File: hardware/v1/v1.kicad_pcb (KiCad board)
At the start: 2 copper layers, 120 x 100 mm, 69 parts, among them J1 AUDIO IN, J2 MIDI OUT, J3 MIDI IN, J4 MIDI THRU, J5 OUTPUT R, J6 OUTPUT L - MONO, J7 EXP 2, J8 EXP 1, J9 Conn_01x02_Female, SW1 RotaryEncoder_Switch, U1 PT8211-pt8211, U2 Pico, U3 2.4inches, U4 TL074, U5 TL074, U6 TL072, U7 6N138

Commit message: started PCB
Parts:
- C1, C10, C11, C12, C13, C14, C15, C16, C17, C18, C19, C2, C20, C21, C22, C23, C24, C4, C5, C6, C7, C8, C9, D1, J7, J8, R1, R10, R11, R12, R13, R14, R15, R16, R17, R18, R19, R2, R20, R3, R4, R5, R6, R7, R8, R9, U4, U5, U6, U7: moved to B.Cu
- J9: footprint Connector_JST:JST_XH_B2B-XH-AM_1x02_P2.50mm_Vertical -> Connector_JST:JST_XH_B2B-XH-A_1x02_P2.50mm_Vertical
- moved U7 351.4 mm to (125.1, 72.7), turned to 180 degrees
- moved AudioIn_gain_trim_R_1 317.8 mm to (118.5, 118.8)
- moved D1 317.1 mm to (127.8, 72.7), turned to -90 degrees
- moved C24 308.9 mm to (114.6, 80.5), turned to 90 degrees
- moved RV_gain_trim_L_1 296.7 mm to (159.0, 67.8)
- moved R10 261.9 mm to (185.3, 92.0), turned to 180 degrees
- moved C12 249.3 mm to (185.6, 88.1), turned to 180 degrees
- moved R12 248.7 mm to (196.3, 66.5), turned to 180 degrees
- moved U4 248.5 mm to (185.5, 69.5), turned to 180 degrees
- moved C1 247.0 mm to (148.2, 108.0), turned to 180 degrees
- moved U6 244.4 mm to (140.7, 104.8)
- moved C11 238.5 mm to (196.3, 88.1), turned to 180 degrees
- moved RV_gain_trim_R_1 221.0 mm to (205.5, 62.8)
- moved U5 192.5 mm to (196.3, 69.5), turned to 180 degrees
- moved R2 183.5 mm to (496.4, 141.9), turned to 180 degrees
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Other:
- board size 120 x 100 mm -> 140 x 100 mm
- board text added: "Batteries (4xAA)"

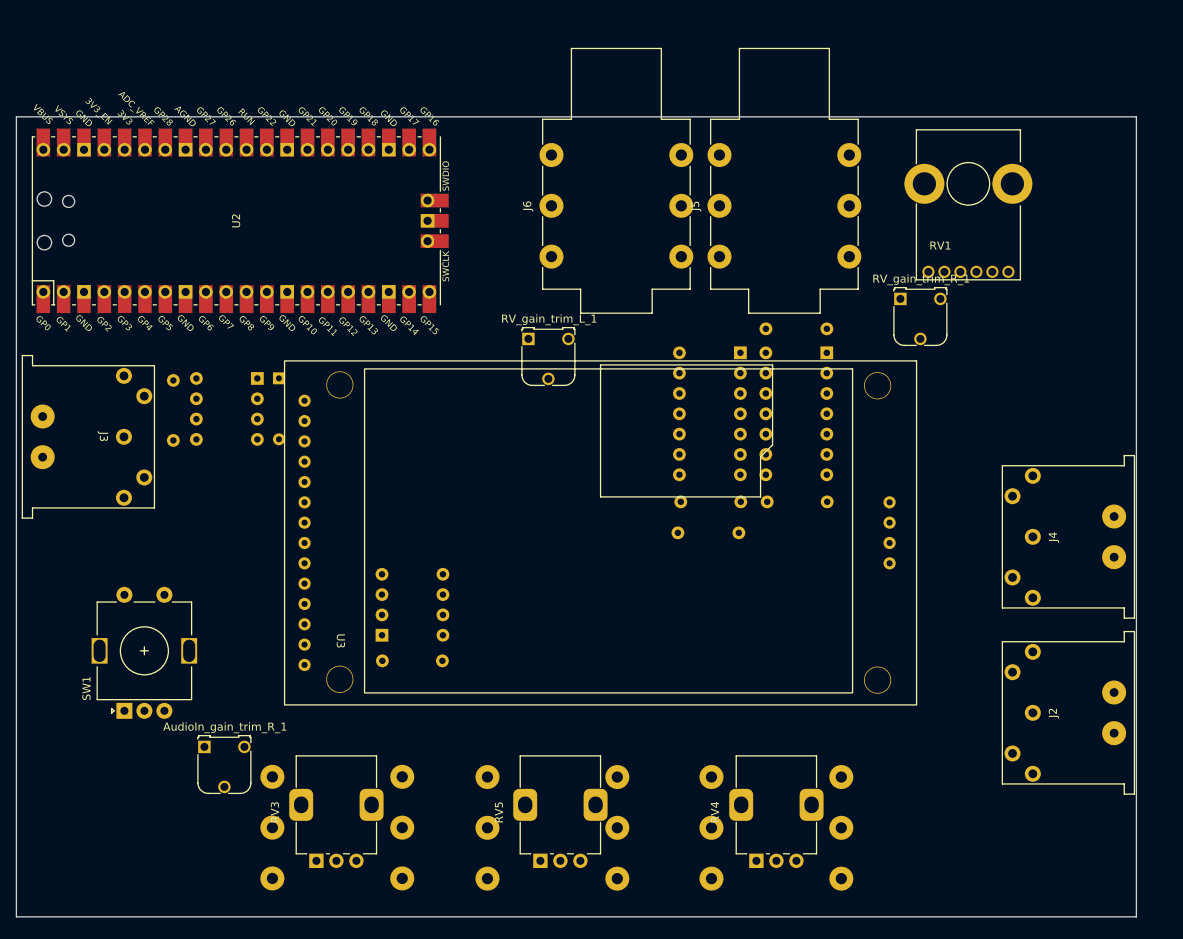
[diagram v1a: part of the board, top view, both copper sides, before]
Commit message: Shifted all connectors to B-side
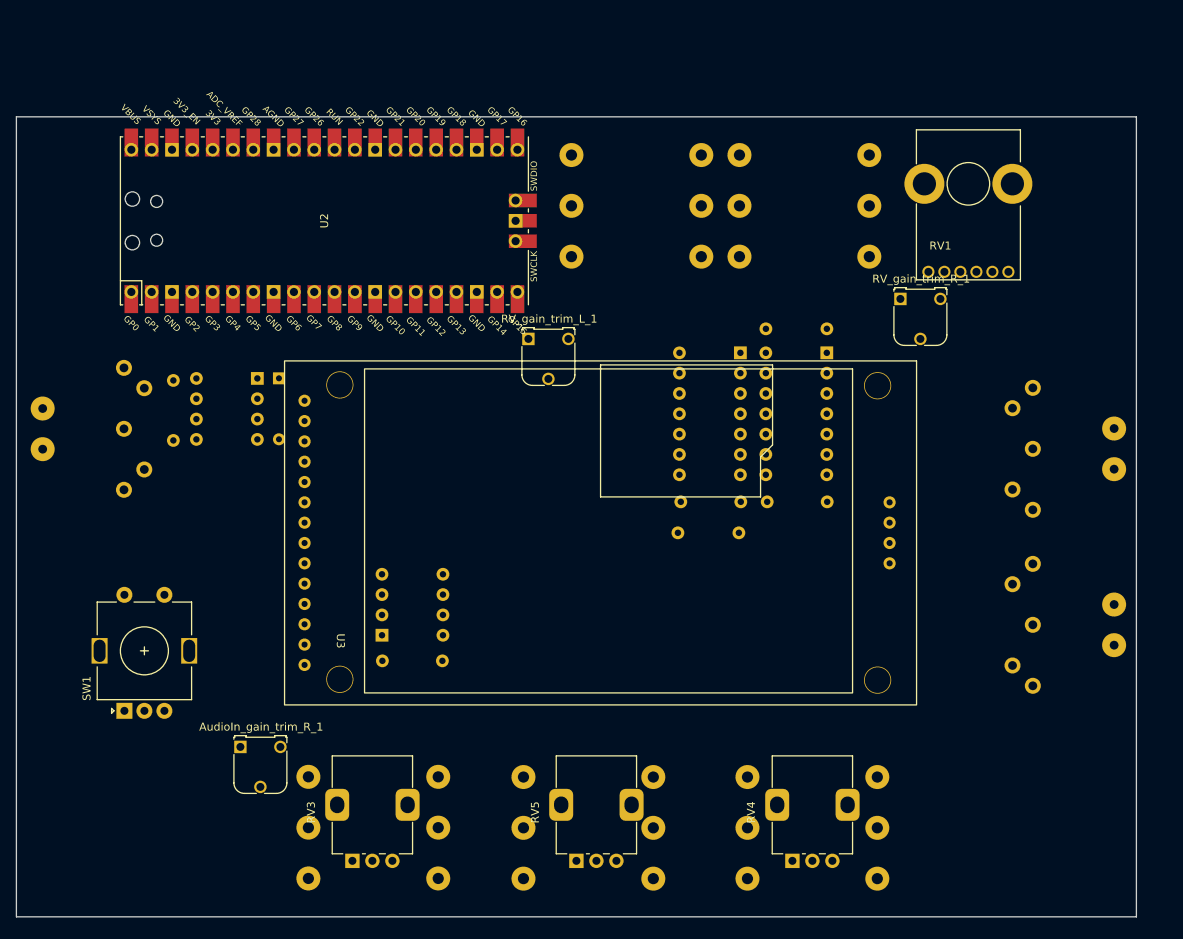
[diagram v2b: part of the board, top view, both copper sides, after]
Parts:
- J2, J3, J4, J5, J6: moved to B.Cu
- moved J5 18.7 mm to (201.6, 57.5)
- moved J6 18.7 mm to (180.6, 57.5)
- moved J2 11.0 mm to (222.1, 103.5), turned to -90 degrees
- moved J4 11.0 mm to (222.1, 81.5), turned to -90 degrees
- moved U2 11.0 mm to (133.5, 53.0)
- moved AudioIn_gain_trim_R_1 4.50 mm to (123.0, 118.8)
- moved J1 4.50 mm to (131.5, 122.5)
- moved J7 4.50 mm to (186.4, 122.5)
- moved J8 4.50 mm to (158.4, 122.5)
- moved RV3 4.50 mm to (137.0, 133.0)
- moved RV4 4.50 mm to (192.0, 133.0)
- moved RV5 4.50 mm to (165.0, 133.0)
- moved J3 1.00 mm to (108.4, 79.0), turned to 90 degrees

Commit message: Continued PCB placing
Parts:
- J9: value Conn_01x02_Female -> Batt In
- moved R13 297.9 mm to (175.8, 67.0)
- moved C23 294.7 mm to (122.2, 86.5)
- moved R18 294.6 mm to (125.3, 69.0)
- moved R7 264.7 mm to (163.5, 74.0), turned to -90 degrees
- moved C14 255.9 mm to (164.0, 88.0), turned to 0 degrees
- moved R9 252.4 mm to (166.5, 74.0), turned to -90 degrees
- moved C16 244.0 mm to (166.2, 84.5)
- moved R15 240.3 mm to (215.5, 107.7), turned to -90 degrees
- moved R20 239.0 mm to (216.0, 66.0), turned to -90 degrees
- moved R16 226.1 mm to (215.5, 105.3), turned to 90 degrees
- moved R6 223.9 mm to (184.0, 74.0), turned to -90 degrees
- moved C10 220.2 mm to (166.5, 91.5)
- moved C15 213.3 mm to (187.7, 84.5)
- moved C21 201.0 mm to (154.3, 105.5), turned to 0 degrees
- moved C13 190.6 mm to (184.9, 87.9), turned to 0 degrees
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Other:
- board text added: "1 - A"
- board text added: "1 - B"
- board text added: "2 - A"
- board text added: "2 - B"
- board text added: "3 - A"
- board text added: "3 - B"

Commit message: First draft on PCB placing
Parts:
- added G***: LOGO, PCB_symbols:owl_F_50x70, F.Cu at (60.5, 175.5)
- C3, U1: moved to B.Cu
- moved R14 330.1 mm to (148.3, 94.0)
- moved R2 322.7 mm to (181.0, 74.0), turned to -90 degrees
- moved R17 313.6 mm to (114.5, 83.3), turned to -90 degrees
- moved R3 297.7 mm to (190.2, 105.5), turned to 0 degrees
- moved C3 290.7 mm to (166.6, 107.5), turned to 0 degrees
- moved U1 283.2 mm to (170.5, 103.0), turned to 180 degrees
- moved R11 233.3 mm to (223.3, 69.8), turned to 90 degrees
- moved C8 217.5 mm to (188.0, 95.0)
- moved R5 217.2 mm to (197.8, 108.9)
- moved R1 205.8 mm to (190.2, 102.0), turned to 0 degrees
- moved C5 192.5 mm to (171.0, 92.8), turned to -90 degrees
- moved C2 191.8 mm to (184.9, 106.5)
- moved C7 186.4 mm to (177.0, 92.8), turned to -90 degrees
- moved C6 149.1 mm to (193.5, 93.0), turned to -90 degrees
- moved C4 147.7 mm to (199.4, 92.9), turned to -90 degrees
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
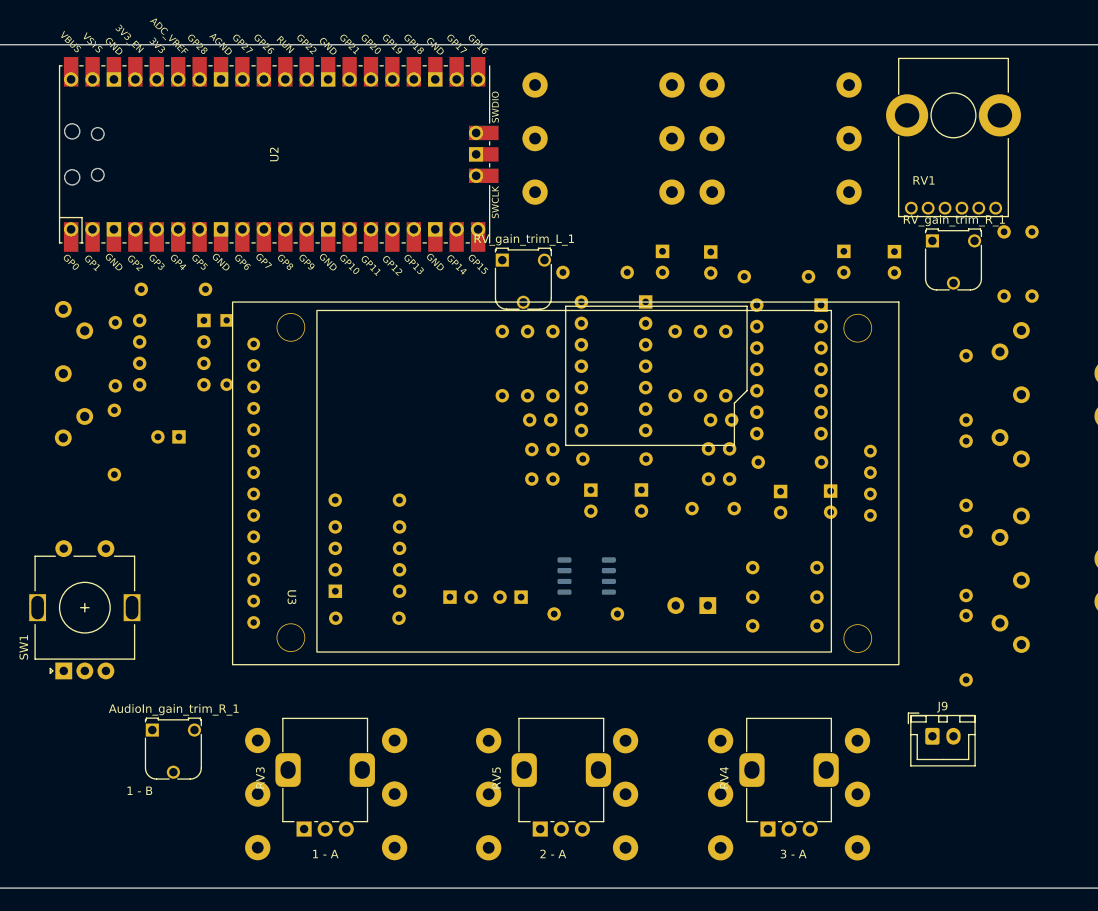
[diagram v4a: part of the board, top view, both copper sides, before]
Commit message: Added mounting holes - Cleaned PCB placement
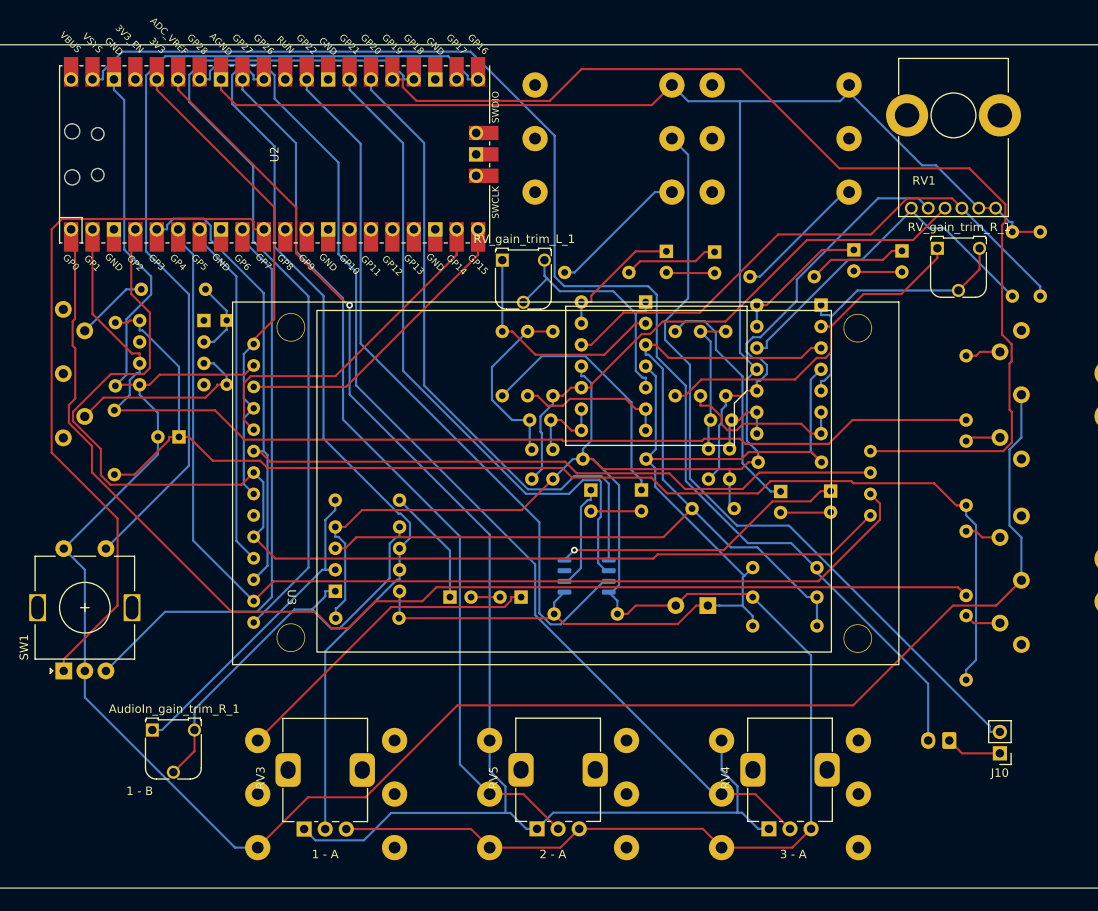
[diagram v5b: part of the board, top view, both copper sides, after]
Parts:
- added J10: Close for battery power, Connector_PinHeader_2.54mm:PinHeader_1x02_P2.54mm_Vertical, F.Cu at (219.5, 124.0)
- J9: moved to B.Cu
- moved J9 2.06 mm to (213.5, 122.5), turned to 180 degrees
- moved C17 1.20 mm to (202.2, 64.3)
- moved RV_gain_trim_R_1 1.06 mm to (212.1, 64.1)
- moved R10 0.98 mm to (221.0, 69.8)
- moved R11 0.98 mm to (224.3, 69.8)
- moved C18 0.89 mm to (207.9, 64.4)
- moved R12 0.68 mm to (197.5, 67.5)
- moved C22 0.45 mm to (185.7, 64.6)
- moved C19 0.45 mm to (180.0, 64.5)
- moved RV5 0.38 mm to (164.6, 133.0)
- moved R13 0.20 mm to (175.5, 67.0)
- moved J7 0.12 mm to (186.5, 122.5)
- moved J8 0.12 mm to (159.0, 122.5)
- moved RV4 0.12 mm to (192.1, 133.0)
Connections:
- J6 pad R: batt- -> Net-(J6-PadR)
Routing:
- net GNDA: track 0.00 -> 366.0 mm
- net GND: track 0.00 -> 255.7 mm
- net ADC_VREF: track 0.00 -> 171.9 mm, vias 0 -> 1
- net batt+: track 0.00 -> 159.9 mm
- net +3.3V: track 0.00 -> 148.2 mm
- net Net-(R16-Pad1): track 0.00 -> 144.4 mm
- net Net-(U2-Pad4): track 0.00 -> 141.8 mm
- net Net-(U2-Pad5): track 0.00 -> 130.0 mm
- net Net-(R17-Pad1): track 0.00 -> 129.8 mm
- net Net-(U2-Pad6): track 0.00 -> 129.6 mm
- net Net-(U2-Pad25): track 0.00 -> 128.8 mm
- net Net-(J7-PadR): track 0.00 -> 128.2 mm
- net filtered_vcc: track 0.00 -> 120.9 mm
- net virtual_mass: track 0.00 -> 110.7 mm
- net Net-(RV3-Pad2): track 0.00 -> 107.5 mm
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
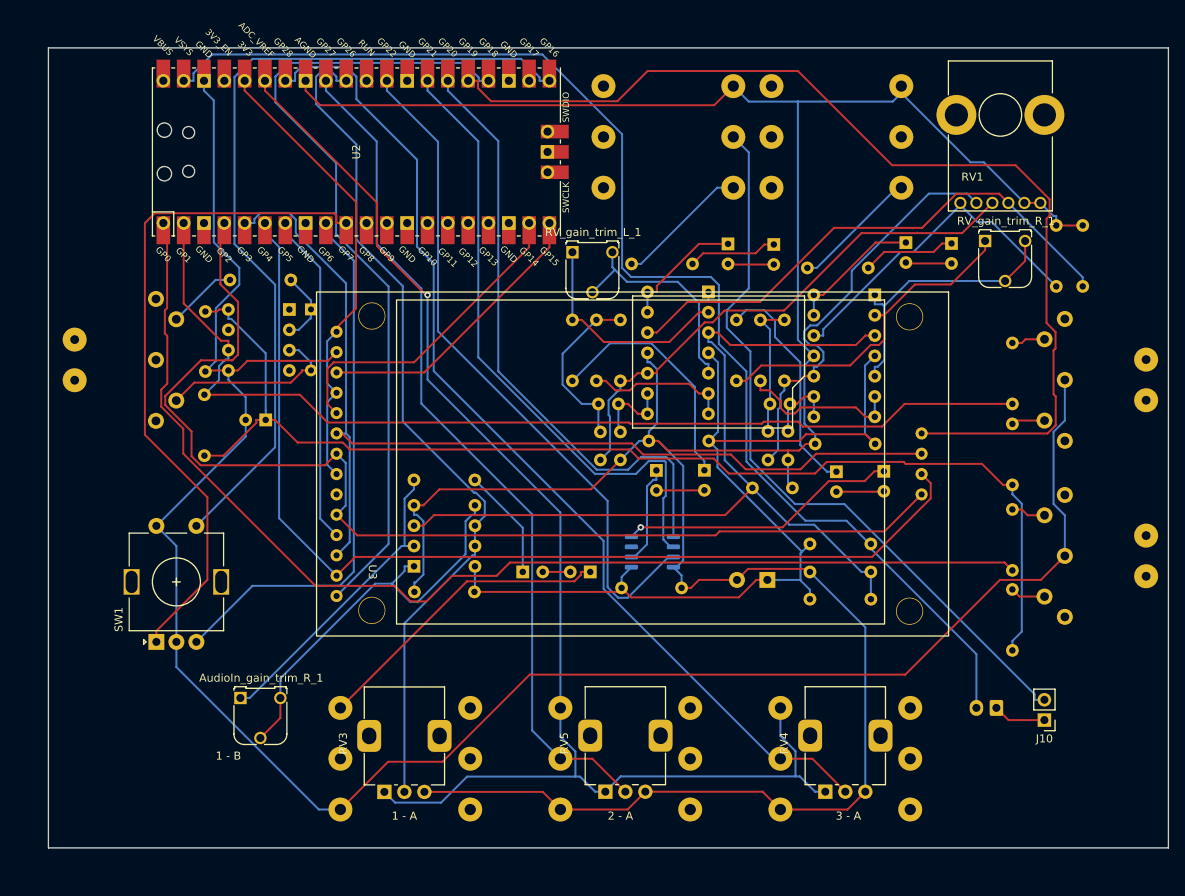
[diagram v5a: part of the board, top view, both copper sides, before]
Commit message: PCB routing and mass planes
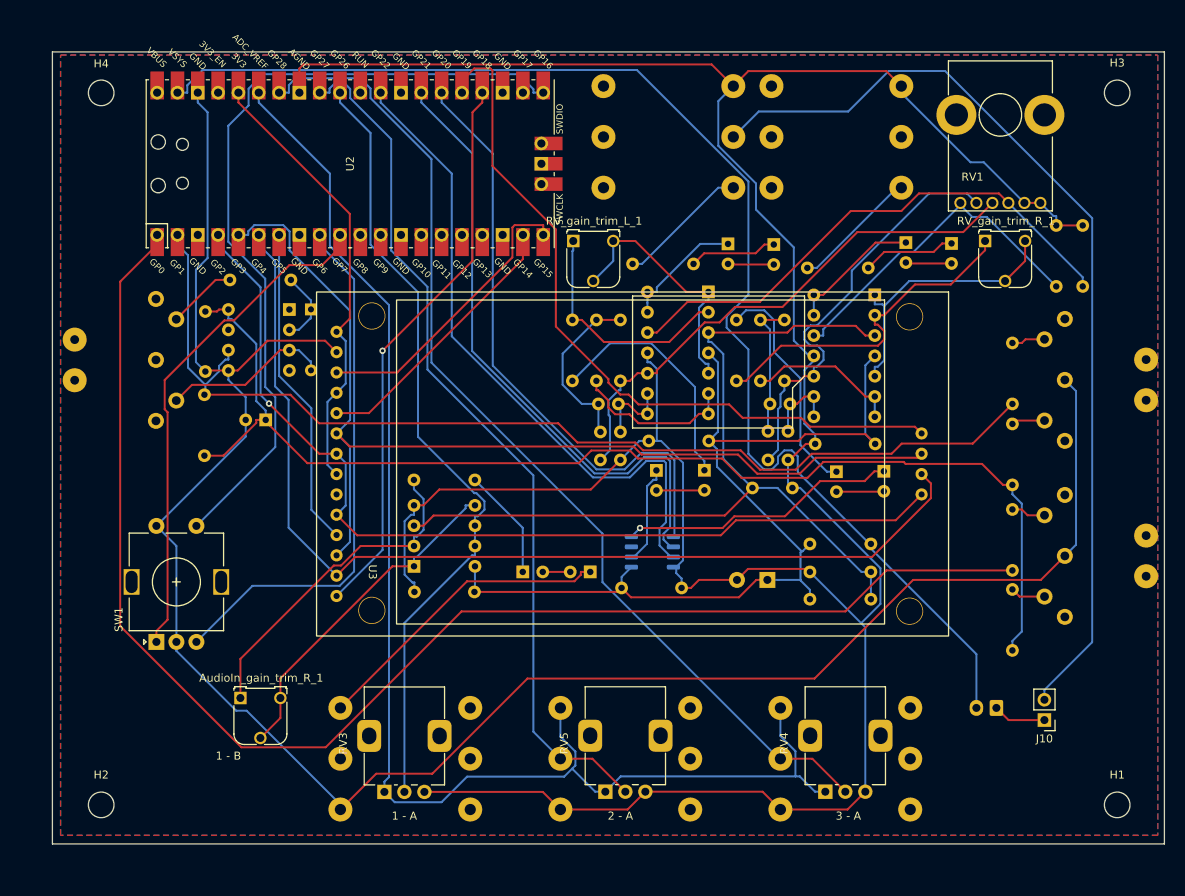
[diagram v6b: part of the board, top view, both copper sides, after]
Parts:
- added H1: MountingHole, MountingHole:MountingHole_3.2mm_M3_ISO14580, F.Cu at (228.6, 134.6)
- added H2: MountingHole, MountingHole:MountingHole_3.2mm_M3_ISO14580, F.Cu at (101.6, 134.6)
- added H3: MountingHole, MountingHole:MountingHole_3.2mm_M3_ISO14580, F.Cu at (228.6, 45.6)
- added H4: MountingHole, MountingHole:MountingHole_3.2mm_M3_ISO14580, F.Cu at (101.6, 45.7)
- moved U2 1.67 mm to (132.7, 54.5)
- moved RV_gain_trim_L_1 1.41 mm to (160.6, 64.1)
- moved R13 0.13 mm to (175.6, 67.0)
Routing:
- net Net-(U2-Pad25): track 128.8 -> 92.9 mm
- net Net-(R16-Pad1): track 144.4 -> 177.8 mm
- net Net-(U2-Pad24): track 102.0 -> 70.5 mm, vias 0 -> 1
- net Net-(J10-Pad2): track 93.1 -> 118.6 mm
- net Net-(U2-Pad4): track 141.8 -> 119.6 mm, vias 0 -> 1
- net Net-(SW1-PadA): track 85.0 -> 63.8 mm
- net GNDA: track 366.0 -> 380.2 mm
- net Net-(AudioIn_gain_trim_R_1-Pad2): track 50.7 -> 42.7 mm
- net Net-(RV3-Pad2): track 107.5 -> 99.6 mm
- net Net-(U2-Pad19): track 40.6 -> 34.3 mm
- net Net-(R17-Pad1): track 129.8 -> 135.5 mm
- net batt+: track 159.9 -> 164.8 mm
- net Net-(AudioIn_gain_trim_R_1-Pad1): track 38.3 -> 41.9 mm
- net Net-(U1-Pad3): track 85.6 -> 82.2 mm
- net GND: track 255.7 -> 252.6 mm
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- added copper zone on F.Cu, net GND
- added copper zone on B.Cu, net GNDA
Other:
- board size 140 x 100 mm -> 139 x 99 mm
